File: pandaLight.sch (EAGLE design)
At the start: 161 parts, among them J1 PJ-037A, U1 MIC23450AAAYML, U10 AS4C128M16D3, U11 PMOD-2X6, U12 PMOD-2X6, U13 PLR135-T10, U14 PLT133-T10W, U15 PLR135-T10, U16 TP10SQ, U17 TP10SQ, U18 PAN1322, U2 6SLX45CSG324, U3 TPD4S014SON, U4 FT2232HL, U5 93LC46BT-I/OT, U6 TPD12S016PWR, U7 TPD12S016PWR, U8 N25Q128AF8, U9 TPD12S016PWR, X1 USBUB-S, X2 HDMI_RECEPTICAL_A, X3 HDMI_RECEPTICAL_A, X4 HDMI_RECEPTICAL_A, Y1 403, Y2 20Mhz

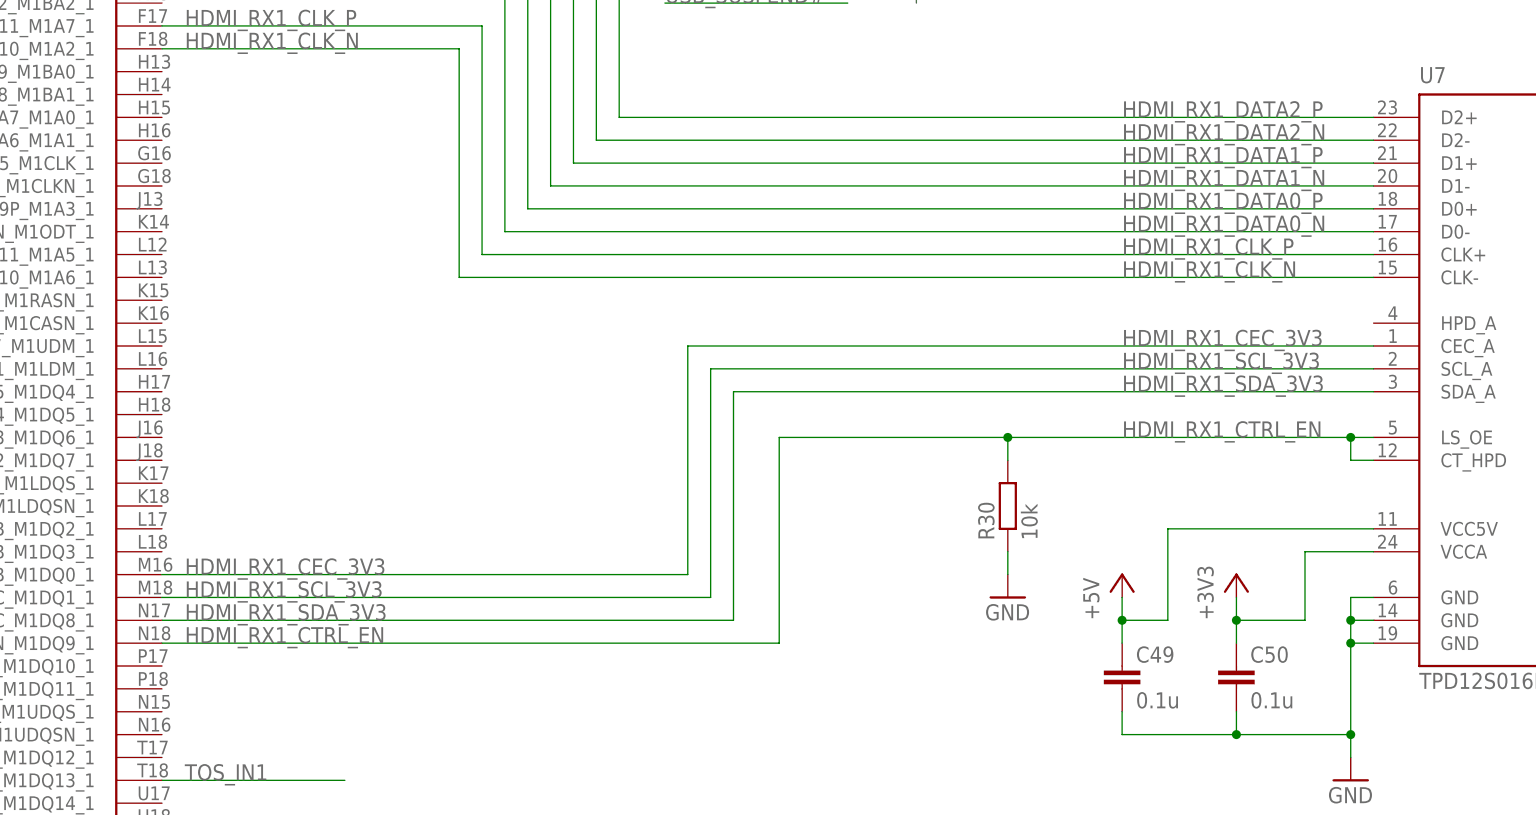
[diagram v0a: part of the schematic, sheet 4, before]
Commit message: Finished first routing of HDMI_RX1; Corrected some traces and placements
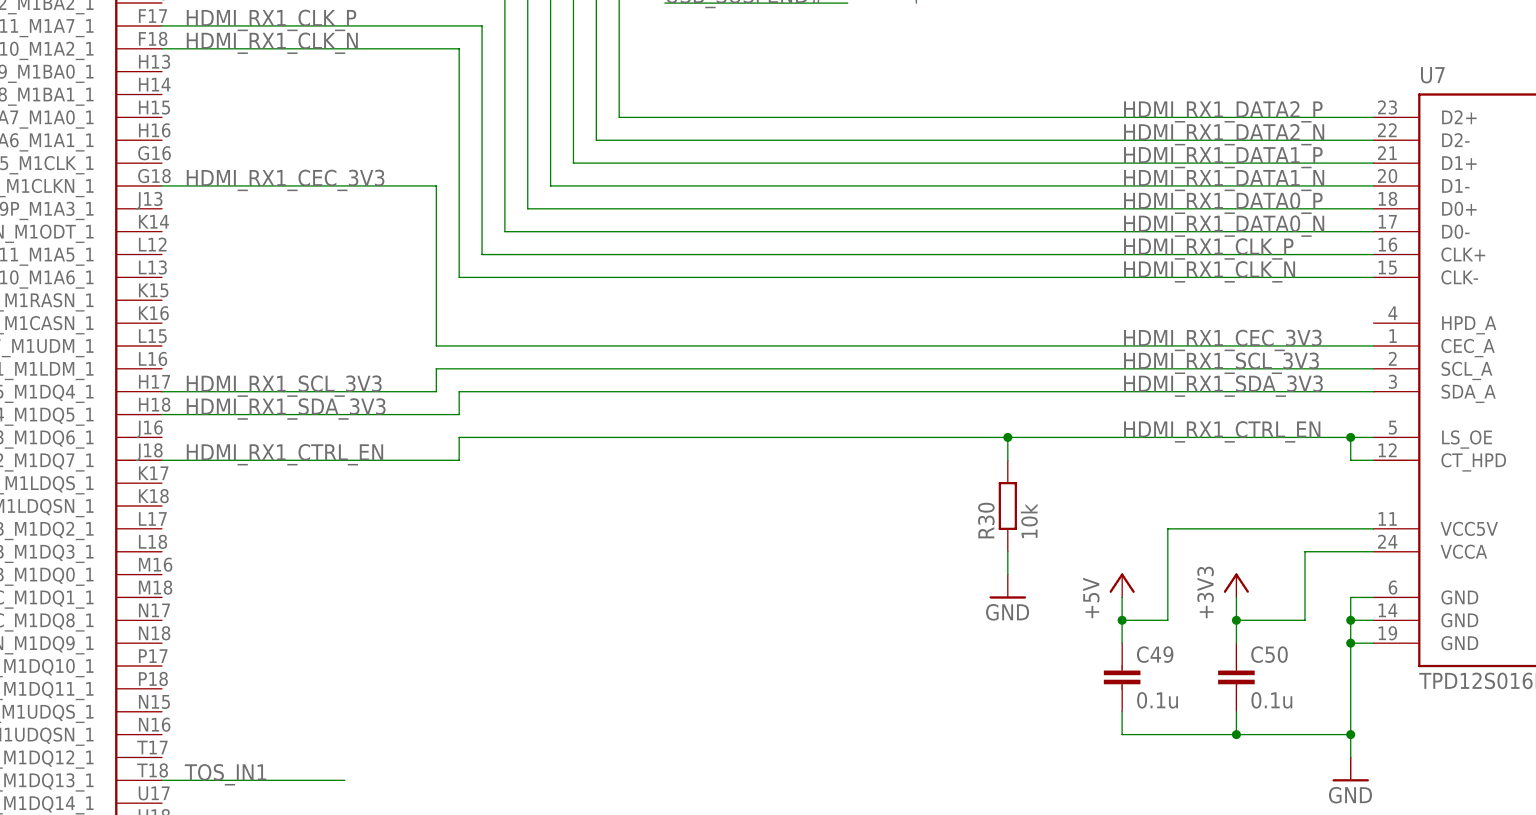
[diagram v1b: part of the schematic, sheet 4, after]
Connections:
- net HDMI_RX1_CEC_3V3: now also U2B1.IO_L38N_A4_M1CLKN_1; no longer U2B1.IO_L47P_FWE_B_M1DQ0_1
- net HDMI_RX1_CTRL_EN: now also U2B1.IO_L44N_A2_M1DQ7_1; no longer U2B1.IO_L48N_M1DQ9_1
- net HDMI_RX1_SCL_3V3: now also U2B1.IO_L43P_GCLK5_M1DQ4_1; no longer U2B1.IO_L47N_LDC_M1DQ1_1
- net HDMI_RX1_SDA_3V3: now also U2B1.IO_L43N_GCLK4_M1DQ5_1; no longer U2B1.IO_L48P_HDC_M1DQ8_1
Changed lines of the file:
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@@
 <pinref part="U7" gate="G$1" pin="CEC_A"/>
 <label x="134.62" y="81.28" size="1.778" layer="95"/>
-<wire x1="162.56" y1="81.28" x2="86.36" y2="81.28" width="0.1524" layer="91"/>
-<wire x1="86.36" y1="81.28" x2="86.36" y2="55.88" width="0.1524" layer="91"/>
-<pinref part="U2" gate="B1" pin="IO_L47P_FWE_B_M1DQ0_1"/>
-<wire x1="86.36" y1="55.88" x2="27.94" y2="55.88" width="0.1524" layer="91"/>
-<label x="30.48" y="55.88" size="1.778" layer="95"/>
+<wire x1="162.56" y1="81.28" x2="58.42" y2="81.28" width="0.1524" layer="91"/>
+<pinref part="U2" gate="B1" pin="IO_L38N_A4_M1CLKN_1"/>
+<wire x1="58.42" y1="81.28" x2="58.42" y2="99.06" width="0.1524" layer="91"/>
+<wire x1="58.42" y1="99.06" x2="27.94" y2="99.06" width="0.1524" layer="91"/>
+<label x="30.48" y="99.06" size="1.778" layer="95"/>
 </segment>
 </net>
@@
 <pinref part="U7" gate="G$1" pin="SCL_A"/>
 <label x="134.62" y="78.74" size="1.778" layer="95"/>
-<wire x1="162.56" y1="78.74" x2="88.9" y2="78.74" width="0.1524" layer="91"/>
-<wire x1="88.9" y1="78.74" x2="88.9" y2="53.34" width="0.1524" layer="91"/>
-<pinref part="U2" gate="B1" pin="IO_L47N_LDC_M1DQ1_1"/>
-<wire x1="88.9" y1="53.34" x2="27.94" y2="53.34" width="0.1524" layer="91"/>
-<label x="30.48" y="53.34" size="1.778" layer="95"/>
+<wire x1="162.56" y1="78.74" x2="58.42" y2="78.74" width="0.1524" layer="91"/>
+<wire x1="58.42" y1="78.74" x2="58.42" y2="76.2" width="0.1524" layer="91"/>
+<pinref part="U2" gate="B1" pin="IO_L43P_GCLK5_M1DQ4_1"/>
+<wire x1="58.42" y1="76.2" x2="27.94" y2="76.2" width="0.1524" layer="91"/>
+<label x="30.48" y="76.2" size="1.778" layer="95"/>
 </segment>
 </net>
@@
 <pinref part="U7" gate="G$1" pin="SDA_A"/>
 <label x="134.62" y="76.2" size="1.778" layer="95"/>
-<wire x1="162.56" y1="76.2" x2="91.44" y2="76.2" width="0.1524" layer="91"/>
-<wire x1="91.44" y1="76.2" x2="91.44" y2="50.8" width="0.1524" layer="91"/>
-<pinref part="U2" gate="B1" pin="IO_L48P_HDC_M1DQ8_1"/>
-<wire x1="91.44" y1="50.8" x2="27.94" y2="50.8" width="0.1524" layer="91"/>
-<label x="30.48" y="50.8" size="1.778" layer="95"/>
+<wire x1="162.56" y1="76.2" x2="60.96" y2="76.2" width="0.1524" layer="91"/>
+<wire x1="60.96" y1="76.2" x2="60.96" y2="73.66" width="0.1524" layer="91"/>
+<pinref part="U2" gate="B1" pin="IO_L43N_GCLK4_M1DQ5_1"/>
+<wire x1="60.96" y1="73.66" x2="27.94" y2="73.66" width="0.1524" layer="91"/>
+<label x="30.48" y="73.66" size="1.778" layer="95"/>
 </segment>
 </net>
@@
 <wire x1="162.56" y1="71.12" x2="160.02" y2="71.12" width="0.1524" layer="91"/>
 <wire x1="160.02" y1="71.12" x2="121.92" y2="71.12" width="0.1524" layer="91"/>
-<wire x1="121.92" y1="71.12" x2="96.52" y2="71.12" width="0.1524" layer="91"/>
-<wire x1="96.52" y1="71.12" x2="96.52" y2="48.26" width="0.1524" layer="91"/>
-<pinref part="U2" gate="B1" pin="IO_L48N_M1DQ9_1"/>
-<wire x1="96.52" y1="48.26" x2="27.94" y2="48.26" width="0.1524" layer="91"/>
-<label x="30.48" y="48.26" size="1.778" layer="95"/>
+<wire x1="121.92" y1="71.12" x2="60.96" y2="71.12" width="0.1524" layer="91"/>
+<wire x1="60.96" y1="71.12" x2="60.96" y2="68.58" width="0.1524" layer="91"/>
+<pinref part="U2" gate="B1" pin="IO_L44N_A2_M1DQ7_1"/>
+<wire x1="60.96" y1="68.58" x2="27.94" y2="68.58" width="0.1524" layer="91"/>
+<label x="30.48" y="68.58" size="1.778" layer="95"/>
 <pinref part="R30" gate="G$1" pin="2"/>
 <wire x1="121.92" y1="68.58" x2="121.92" y2="71.12" width="0.1524" layer="91"/>

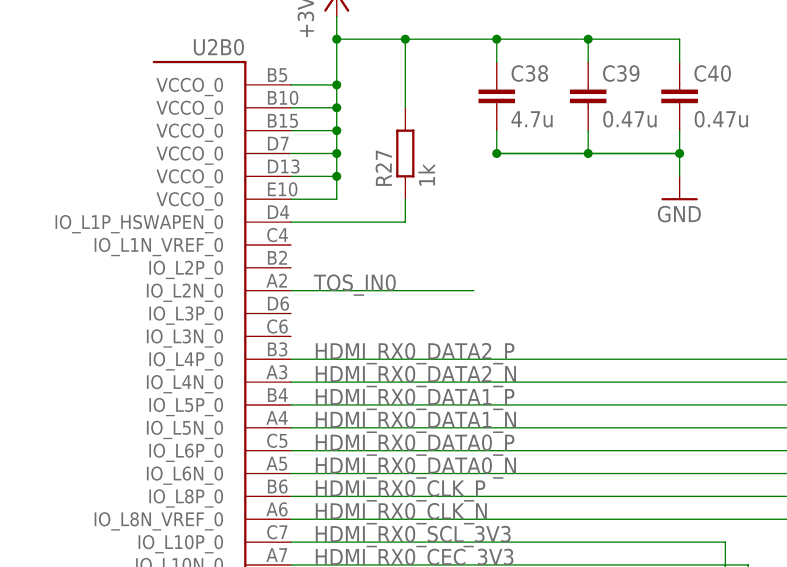
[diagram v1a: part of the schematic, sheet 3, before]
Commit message: Actually resized the board; Tweaked some FT223H related traces
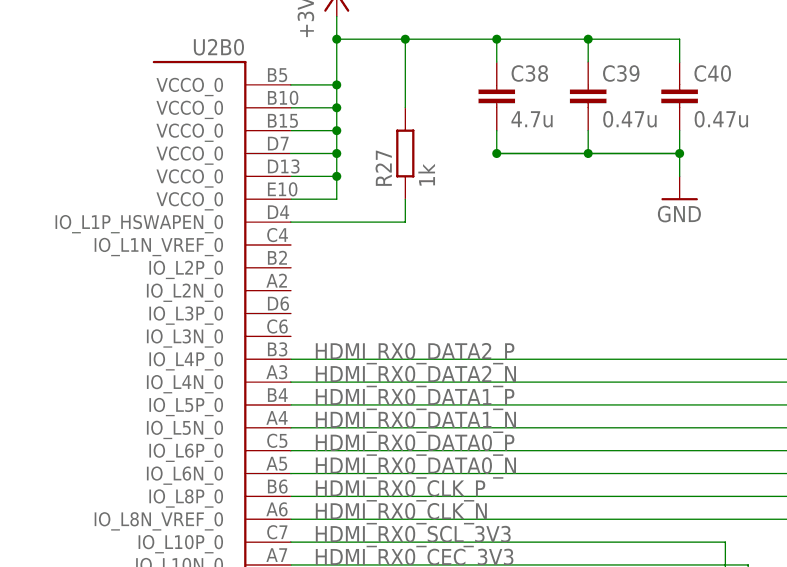
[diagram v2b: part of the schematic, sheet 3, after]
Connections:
- net TOS_IN0: no longer U2B0.IO_L2N_0
- net TOS_IN1: no longer U2B1.IO_L51N_M1DQ13_1
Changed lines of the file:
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@@
-</segment>
-</net>
-<net name="TOS_IN0" class="0">
-<segment>
-<pinref part="U2" gate="B0" pin="IO_L2N_0"/>
-<wire x1="27.94" y1="119.38" x2="48.26" y2="119.38" width="0.1524" layer="91"/>
-<label x="30.48" y="119.38" size="1.778" layer="95"/>
 </segment>
 </net>
@@
 </segment>
 </net>
-<net name="TOS_IN1" class="0">
-<segment>
-<pinref part="U2" gate="B1" pin="IO_L51N_M1DQ13_1"/>
-<wire x1="27.94" y1="33.02" x2="48.26" y2="33.02" width="0.1524" layer="91"/>
-<label x="30.48" y="33.02" size="1.778" layer="95"/>
-</segment>
-</net>

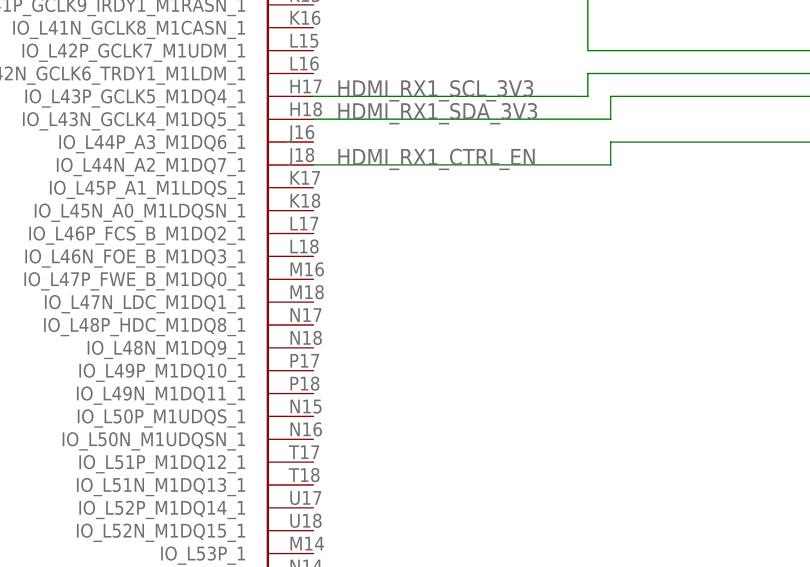
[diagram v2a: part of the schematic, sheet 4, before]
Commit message: Routed blutooth module
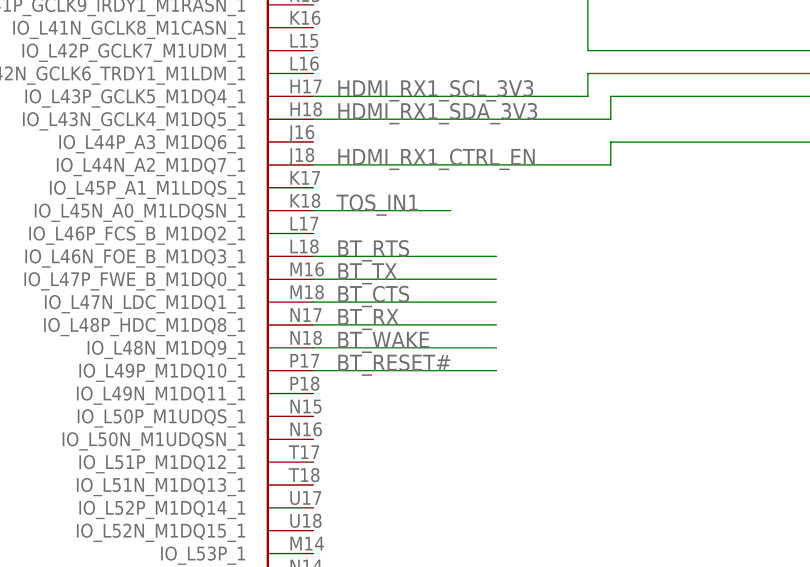
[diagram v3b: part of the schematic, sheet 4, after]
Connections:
- net BT_CTS: now also U2B1.IO_L47N_LDC_M1DQ1_1; no longer U2B2.IO_L63N_2
- net BT_RESET#: now also U2B1.IO_L49P_M1DQ10_1; no longer U2B2.IO_L49N_D4_2
- net BT_RTS: now also U2B1.IO_L46N_FOE_B_M1DQ3_1; no longer U2B2.IO_L63P_2
- net BT_RX: now also U2B1.IO_L48P_HDC_M1DQ8_1; no longer U2B2.IO_L62N_D6_2
- net BT_TX: now also U2B1.IO_L47P_FWE_B_M1DQ0_1; no longer U2B2.IO_L62P_D5_2
- net BT_WAKE: now also U2B1.IO_L48N_M1DQ9_1; no longer U2B2.IO_L49P_D3_2
- net TOS_IN0: now also U2B0.IO_L66N_SCP0_0
- net TOS_IN1: now also U2B1.IO_L45N_A0_M1LDQSN_1
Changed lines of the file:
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@@
+</segment>
+</net>
+<net name="TOS_IN0" class="0">
+<segment>
+<pinref part="U2" gate="B0" pin="IO_L66N_SCP0_0"/>
+<wire x1="27.94" y1="12.7" x2="43.18" y2="12.7" width="0.1524" layer="91"/>
+<label x="30.48" y="12.7" size="1.778" layer="95"/>
 </segment>
 </net>
@@
 <wire x1="83.82" y1="119.38" x2="104.14" y2="119.38" width="0.1524" layer="91"/>
 <label x="83.82" y="119.38" size="1.778" layer="95"/>
+</segment>
+</net>
+<net name="TOS_IN1" class="0">
+<segment>
+<pinref part="U2" gate="B1" pin="IO_L45N_A0_M1LDQSN_1"/>
+<wire x1="27.94" y1="63.5" x2="43.18" y2="63.5" width="0.1524" layer="91"/>
+<label x="30.48" y="63.5" size="1.778" layer="95"/>
+</segment>
+</net>
+<net name="BT_RX" class="0">
+<segment>
+<wire x1="27.94" y1="50.8" x2="48.26" y2="50.8" width="0.1524" layer="91"/>
+<label x="30.48" y="50.8" size="1.778" layer="95"/>
+<pinref part="U2" gate="B1" pin="IO_L48P_HDC_M1DQ8_1"/>
+</segment>
+</net>
+<net name="BT_RTS" class="0">
+<segment>
+<wire x1="27.94" y1="58.42" x2="48.26" y2="58.42" width="0.1524" layer="91"/>
+<label x="30.48" y="58.42" size="1.778" layer="95"/>
+<pinref part="U2" gate="B1" pin="IO_L46N_FOE_B_M1DQ3_1"/>
+</segment>
+</net>
+<net name="BT_CTS" class="0">
+<segment>
+<wire x1="27.94" y1="53.34" x2="48.26" y2="53.34" width="0.1524" layer="91"/>
+<label x="30.48" y="53.34" size="1.778" layer="95"/>
+<pinref part="U2" gate="B1" pin="IO_L47N_LDC_M1DQ1_1"/>
+</segment>
+</net>
+<net name="BT_TX" class="0">
+<segment>
+<wire x1="27.94" y1="55.88" x2="48.26" y2="55.88" width="0.1524" layer="91"/>
+<label x="30.48" y="55.88" size="1.778" layer="95"/>
+<pinref part="U2" gate="B1" pin="IO_L47P_FWE_B_M1DQ0_1"/>
+</segment>
+</net>
+<net name="BT_WAKE" class="0">
+<segment>
+<wire x1="27.94" y1="48.26" x2="48.26" y2="48.26" width="0.1524" layer="91"/>
+<label x="30.48" y="48.26" size="1.778" layer="95"/>
+<pinref part="U2" gate="B1" pin="IO_L48N_M1DQ9_1"/>
+</segment>
+</net>
+<net name="BT_RESET#" class="0">
+<segment>
+<wire x1="27.94" y1="45.72" x2="48.26" y2="45.72" width="0.1524" layer="91"/>
+<label x="30.48" y="45.72" size="1.778" layer="95"/>
+<pinref part="U2" gate="B1" pin="IO_L49P_M1DQ10_1"/>
 </segment>
 </net>
@@
 </segment>
 </net>
-<net name="BT_RX" class="0">
-<segment>
-<pinref part="U2" gate="B2" pin="IO_L62N_D6_2"/>
-<wire x1="40.64" y1="25.4" x2="60.96" y2="25.4" width="0.1524" layer="91"/>
-<label x="43.18" y="25.4" size="1.778" layer="95"/>
-</segment>
-</net>
-<net name="BT_RTS" class="0">
-<segment>
-<pinref part="U2" gate="B2" pin="IO_L63P_2"/>
-<wire x1="40.64" y1="22.86" x2="60.96" y2="22.86" width="0.1524" layer="91"/>
-<label x="43.18" y="22.86" size="1.778" layer="95"/>
-</segment>
-</net>
-<net name="BT_CTS" class="0">
-<segment>
-<pinref part="U2" gate="B2" pin="IO_L63N_2"/>
-<wire x1="40.64" y1="20.32" x2="60.96" y2="20.32" width="0.1524" layer="91"/>
-<label x="43.18" y="20.32" size="1.778" layer="95"/>
-</segment>
-</net>
-<net name="BT_TX" class="0">
-<segment>
-<pinref part="U2" gate="B2" pin="IO_L62P_D5_2"/>
-<wire x1="40.64" y1="27.94" x2="60.96" y2="27.94" width="0.1524" layer="91"/>
-<label x="43.18" y="27.94" size="1.778" layer="95"/>
-</segment>
-</net>
-<net name="BT_WAKE" class="0">
-<segment>
-<pinref part="U2" gate="B2" pin="IO_L49P_D3_2"/>
-<wire x1="40.64" y1="33.02" x2="60.96" y2="33.02" width="0.1524" layer="91"/>
-<label x="43.18" y="33.02" size="1.778" layer="95"/>
-</segment>
-</net>
-<net name="BT_RESET#" class="0">
-<segment>
-<pinref part="U2" gate="B2" pin="IO_L49N_D4_2"/>
-<wire x1="40.64" y1="30.48" x2="60.96" y2="30.48" width="0.1524" layer="91"/>
-<label x="43.18" y="30.48" size="1.778" layer="95"/>
-</segment>
-</net>
